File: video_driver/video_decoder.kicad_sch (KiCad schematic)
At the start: 1 part, among them U2 ADV7180BCPZ

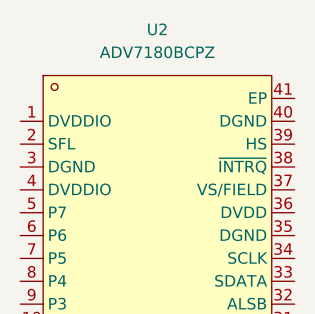
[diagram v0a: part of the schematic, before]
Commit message: power supply start
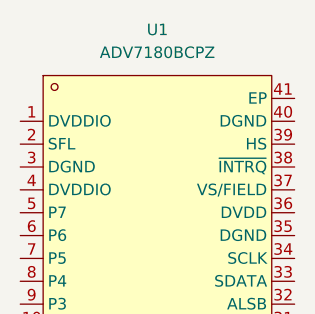
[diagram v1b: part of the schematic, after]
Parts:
- renumbered U2 to U1
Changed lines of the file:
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@@
 		(dnp no)
 		(fields_autoplaced yes)
-		(property "Reference" "U2"
+		(property "Reference" "U1"
 			(at 190.5 93.98 0)
 			(show_name no)
@@
 		(instances
 			(project "video_driver"
-				(path "/4e065576-da6f-4368-b927-7308aa4f3ebd"
-					(reference "U2")
+				(path "/4e065576-da6f-4368-b927-7308aa4f3ebd/151a68a5-9bf1-4690-afb2-c9d2378ba2be"
+					(reference "U1")
 					(unit 1)
 				)
-				(path "/4e065576-da6f-4368-b927-7308aa4f3ebd/151a68a5-9bf1-4690-afb2-c9d2378ba2be"
-					(reference "U2")
-					(unit 1)
-				)

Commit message: power supply work
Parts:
- added C10, C11, C12, C13: 0u1, symbol Device:C
- added C14: 10n, symbol Device:C
- added F3: Fuse, symbol Device:Fuse
- added R8: 1M, symbol Device:R
- added Y1: 28.63636, symbol Device:Crystal
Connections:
- net +3V3: now reaches U1.1 (DVDDIO)
- net +3V3: now also U1.4 (DVDDIO)
- net P2: now reaches U1.10 (P2)
- net at U1.12 (XTAL1): now also C11.2, R8.1, Y1.1
- net at U1.13 (XTAL): now also C12.2, R8.2, Y1.2
- net +1V8: now reaches U1.14 (DVDD)
- net +1V8: now also U1.20 (PVDD), U1.27 (AVDD), U1.36 (DVDD), C13.1, C14.1
- net GND: now reaches U1.15 (DGND)
- net GND: now also U1.22 (TEST_0), U1.3 (DGND), U1.35 (DGND), U1.40 (DGND), U1.41 (EP), C11.1, C12.1, C13.2, C14.2
- net P1: now reaches U1.16 (P1)
- net P0: now reaches U1.17 (P0)
- net ~{PWRDWN}: now reaches U1.18 (~{PWRDWN})
- net AGND: now reaches U1.21 (AGND)
- net AGND: now also U1.24 (AGND), U1.28 (AGND)
- net AIN1: now reaches U1.23 (AIN1)
- net at U1.25 (VREFP): now also C10.2
- net at U1.26 (VREFN): now also C10.1
- net AIN2: now reaches U1.29 (AIN2)
- net AIN3: now reaches U1.30 (AIN3)
- net ~{RESET}: now reaches U1.31 (~{RESET})
- net P7: now reaches U1.5 (P7)
- net P6: now reaches U1.6 (P6)
- net P5: now reaches U1.7 (P5)
- net P4: now reaches U1.8 (P4)
- net P3: now reaches U1.9 (P3)

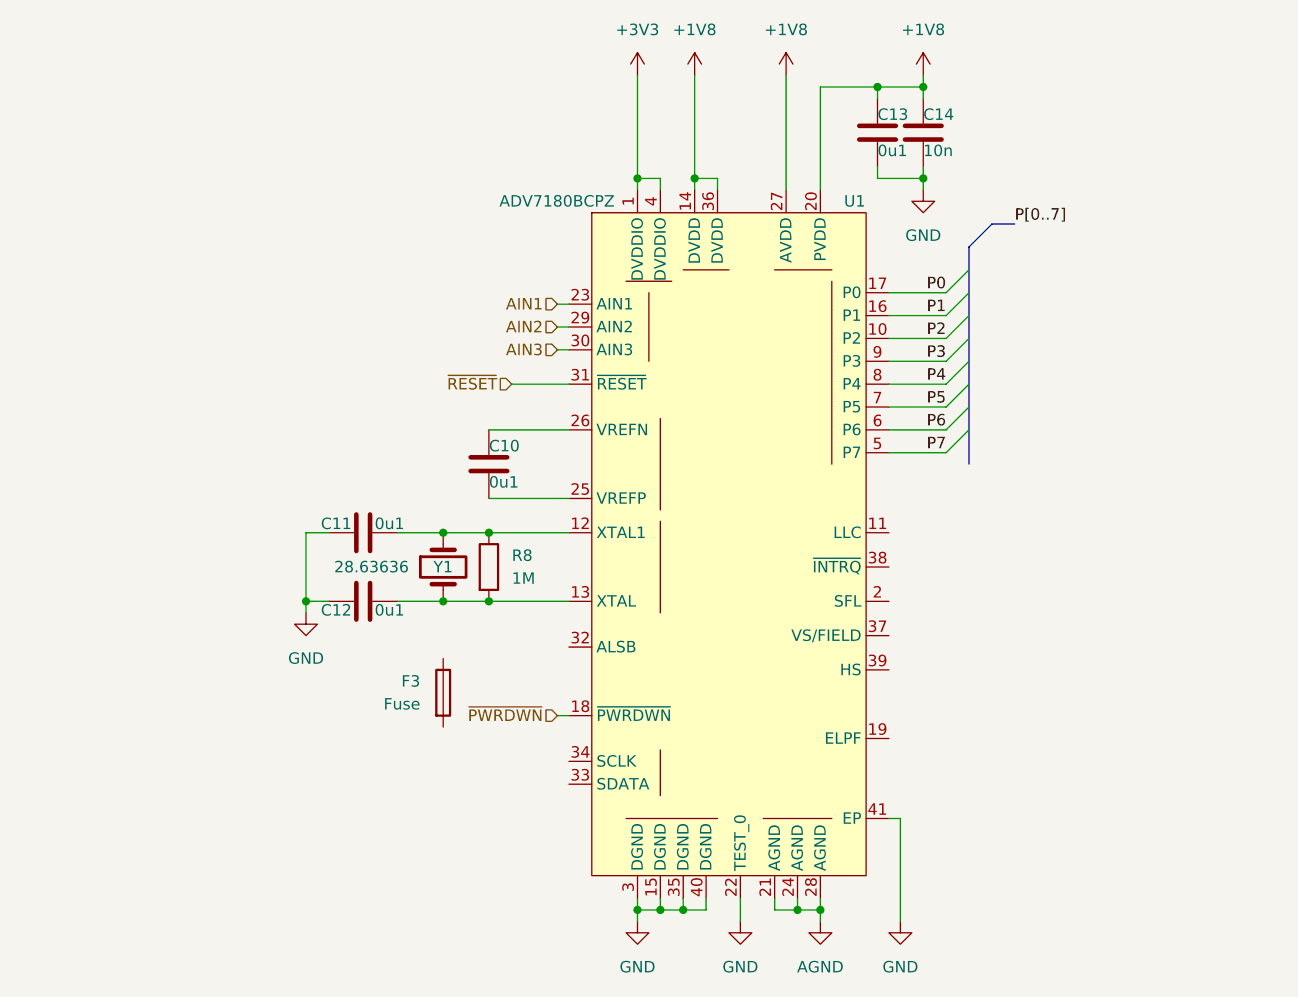
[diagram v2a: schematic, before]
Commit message: new mcu
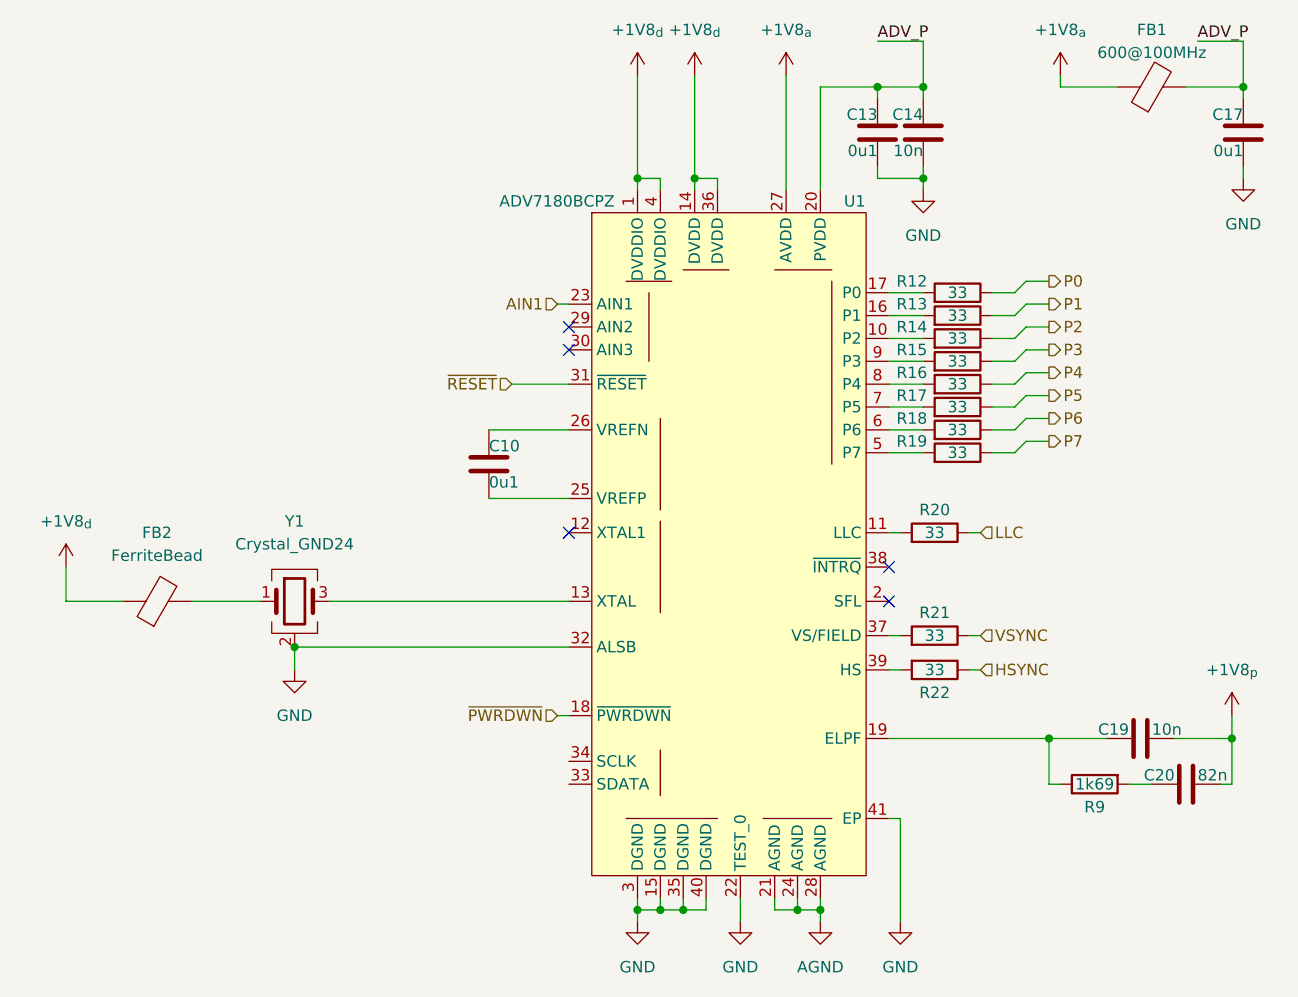
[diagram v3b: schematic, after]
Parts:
- removed C11, C12: 0u1, symbol Device:C
- removed F3: Fuse, symbol Device:Fuse
- removed R8: 1M, symbol Device:R
- removed Y1: 28.63636, symbol Device:Crystal
- added C17: 0u1, Capacitor_SMD:C_0603_1608Metric, symbol Device:C
- added C19: 10n, Capacitor_SMD:C_0603_1608Metric, symbol Device:C
- added C20: 82n, Capacitor_SMD:C_0603_1608Metric, symbol Device:C
- added FB1: 600@100MHz, symbol Device:FerriteBead
- added FB2: FerriteBead, symbol Device:FerriteBead
- added R12, R13, R14, R15, R16, R17, R18, R19, R20, R21, R22: 33, Resistor_SMD:R_0402_1005Metric, symbol Device:R
- added R9: 1k69, Resistor_SMD:R_0402_1005Metric, symbol Device:R
- added Y1: Crystal_GND24, symbol Device:Crystal_GND24
- C10, C13, C14: footprint (none) -> Capacitor_SMD:C_0603_1608Metric
- U1: footprint EasyEDA:LFCSP-40_L6.0-W6.0-P0.50-BL-EP -> Package_CSP:LFCSP-40-1EP_6x6mm_P0.5mm_EP4.6x4.6mm
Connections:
- net GND: now also U1.32 (ALSB), C17.2, Y1.2 (G), Y1.4 (G)
- net P0: now also R12.1; no longer U1.17 (P0)
- net P1: now also R13.1; no longer U1.16 (P1)
- net P2: now also R14.1; no longer U1.10 (P2)
- net P3: now also R15.1; no longer U1.9 (P3)
- net P4: now also R16.1; no longer U1.8 (P4)
- net P5: now also R17.1; no longer U1.7 (P5)
- net P6: now also R18.1; no longer U1.6 (P6)
- net P7: now also R19.1; no longer U1.5 (P7)
- net at U1.13 (XTAL): now also Y1.3
- net at U1.11 (LLC): now also R20.2
- net at U1.19 (ELPF): now also C19.1, R9.1
- net at U1.37 (VS/FIELD): now also R21.2
- net at U1.39 (HS): now also R22.2
- net +1V8 renamed ADV_P
- net ADV_P: now also C17.1, FB1.2; no longer U1.14 (DVDD), U1.27 (AVDD), U1.36 (DVDD)
- net +3V3 renamed +1V8_{d}
- net +1V8_{d}: now also U1.14 (DVDD), U1.36 (DVDD), FB2.1
- net AIN2: no longer names the net of U1.29 (AIN2)
- net AIN3: no longer names the net of U1.30 (AIN3)
- new net: R16.2, U1.8 (P4)
- new net: R14.2, U1.10 (P2)
- new net: R13.2, U1.16 (P1)
- new net: R17.2, U1.7 (P5)
- new net: FB2.2, Y1.1
- new net: R18.2, U1.6 (P6)
- new net: R15.2, U1.9 (P3)
- new net: R19.2, U1.5 (P7)
- new net: R12.2, U1.17 (P0)
- new net: C20.1, R9.2
- new net +1V8_{a}: FB1.1, U1.27 (AVDD)
- new net +1V8_{p}: C19.2, C20.2
- new net HSYNC: R22.1
- new net LLC: R20.1
- new net VSYNC: R21.1
- no-connect marks 0 -> 5
